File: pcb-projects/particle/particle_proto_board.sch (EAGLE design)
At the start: 53 parts, among them IC1 ATTINY20-MMH, IC2 DMC2400V, IC3 DMC2400V, SW1 SW1, SW2 SW2, SW3 SW3

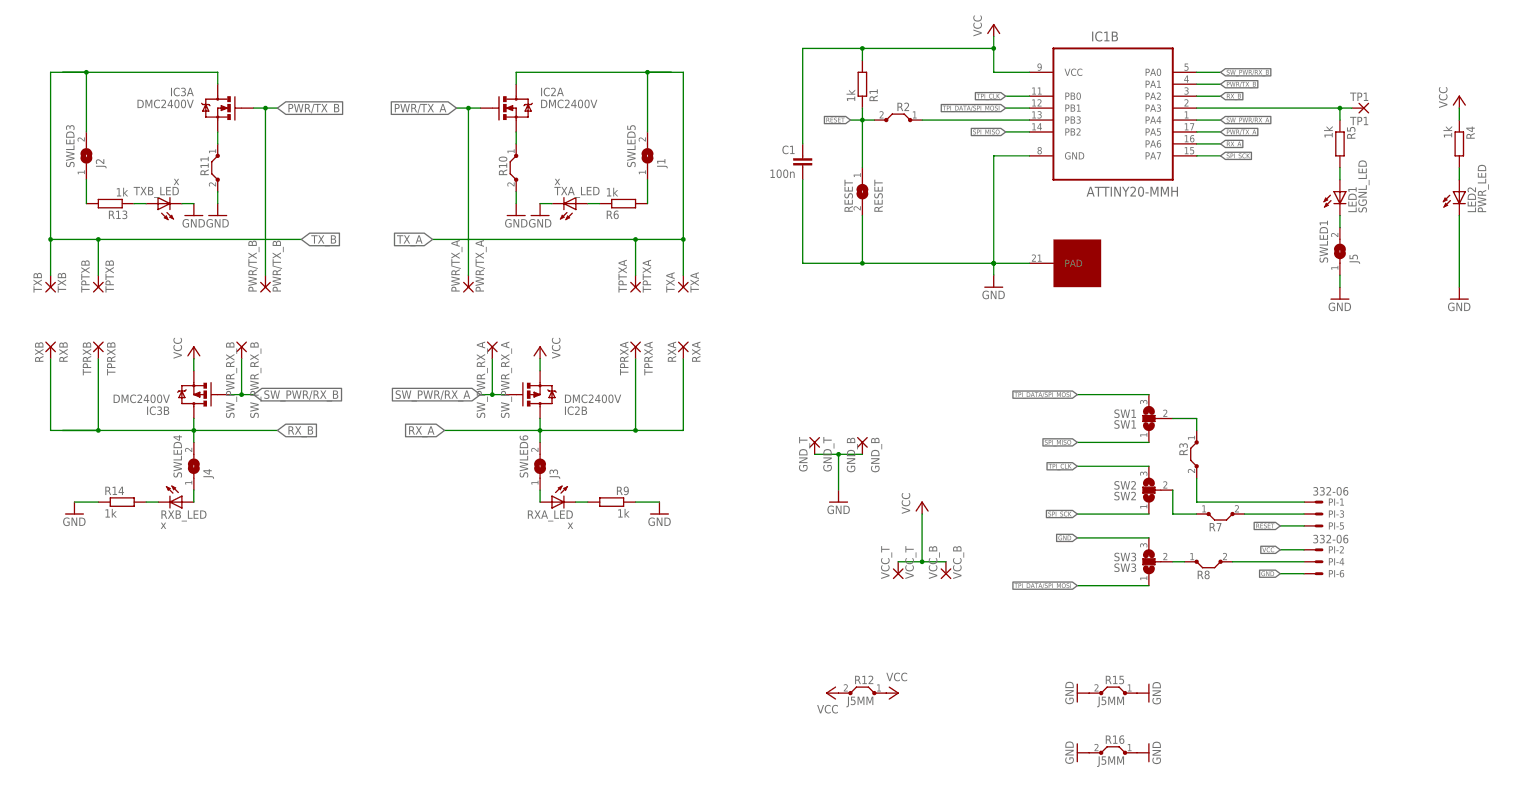
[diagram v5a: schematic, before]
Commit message: set values to all leds, renamed gnd/vcc pads, TX/RX description beside pads, placed vcc/gnd shunts exposed on schema
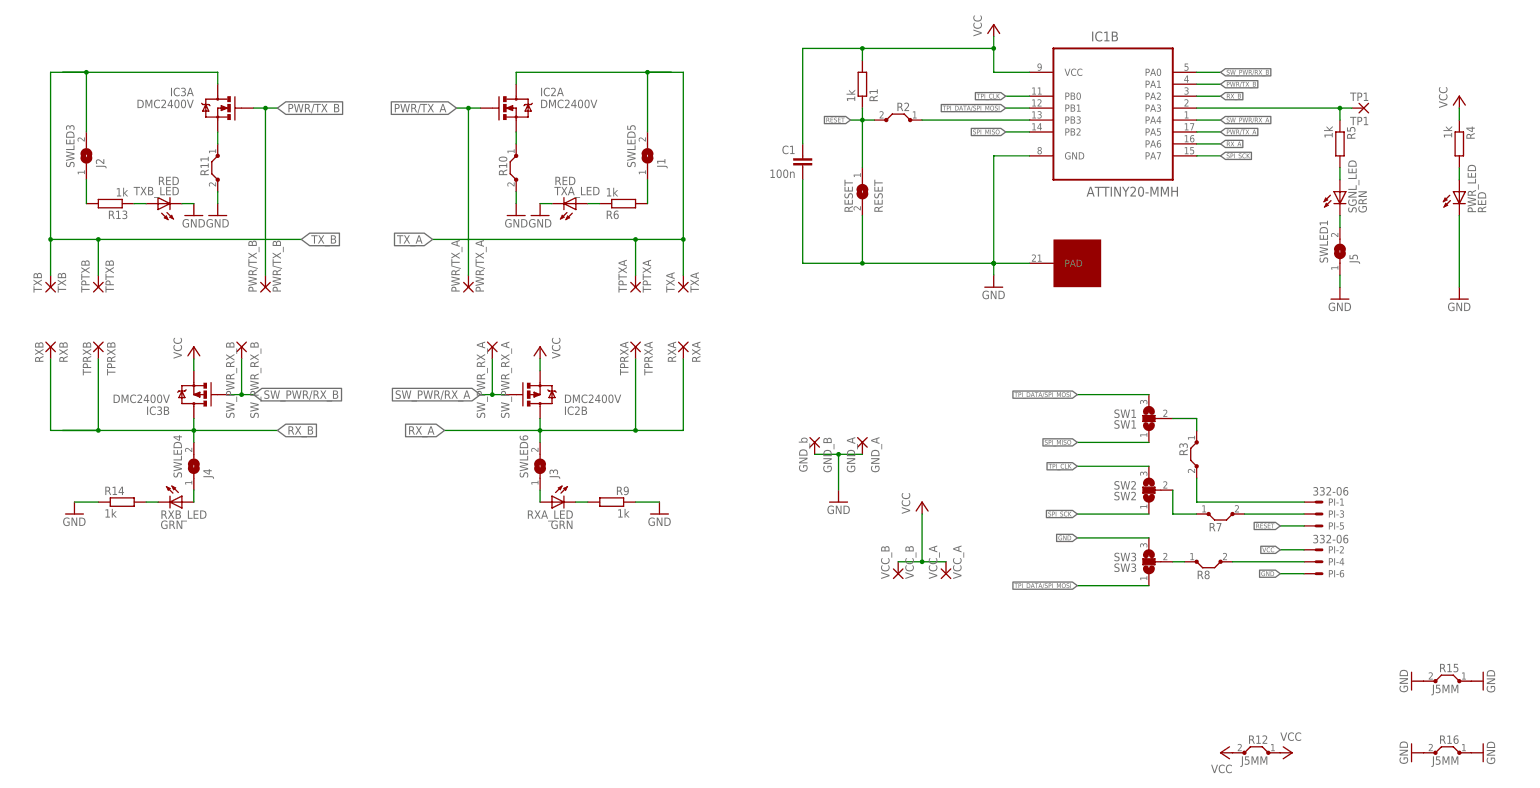
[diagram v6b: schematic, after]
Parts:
- removed GND_T: GND_T, wirepad:1,6/0,9
- removed VCC_T: VCC_T, wirepad:1,6/0,9
- added GND_A: GND_A, wirepad:1,6/0,9
- added VCC_A: VCC_A, wirepad:1,6/0,9
- GND_B: value GND_B -> GND_b
- PWR_LED: value PWR_LED -> RED
- RXA_LED, RXB_LED: value x -> GRN
- SGNL_LED: value SGNL_LED -> GRN
- TXA_LED, TXB_LED: value x -> RED
- renumbered LED1 to SGNL_LED, LED2 to PWR_LED
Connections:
- net GND: now also GND_A.P; no longer GND_T.P
- net VCC: now also VCC_A.P; no longer VCC_T.P
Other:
- note added: "SHUNTS"
- moved on the sheet: GND_B, R12, R15, R16, VCC_B
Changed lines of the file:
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@@
 <part name="R5" library="rcl" deviceset="R-EU_" device="R2010" value="1k"/>
 <part name="GND16" library="supply1" deviceset="GND" device=""/>
-<part name="LED1" library="led" deviceset="LED" device="SML1206" value="SGNL_LED"/>
+<part name="SGNL_LED" library="led" deviceset="LED" device="SML1206" value="GRN"/>
 <part name="P+2" library="supply1" deviceset="VCC" device=""/>
 <part name="IC3" library="diodes" deviceset="DMC2400V" device=""/>
@@
 <part name="R13" library="rcl" deviceset="R-EU_" device="R2010" value="1k"/>
 <part name="GND4" library="supply1" deviceset="GND" device=""/>
-<part name="TXB_LED" library="led" deviceset="LED" device="SML1206" value="x"/>
-<part name="RXB_LED" library="led" deviceset="LED" device="SML1206" value="x"/>
+<part name="TXB_LED" library="led" deviceset="LED" device="SML1206" value="RED"/>
+<part name="RXB_LED" library="led" deviceset="LED" device="SML1206" value="GRN"/>
 <part name="R14" library="rcl" deviceset="R-EU_" device="R2010" value="1k"/>
 <part name="GND5" library="supply1" deviceset="GND" device=""/>
@@
 <part name="R6" library="rcl" deviceset="R-EU_" device="R2010" value="1k"/>
 <part name="GND6" library="supply1" deviceset="GND" device=""/>
-<part name="TXA_LED" library="led" deviceset="LED" device="SML1206" value="x"/>
-<part name="RXA_LED" library="led" deviceset="LED" device="SML1206" value="x"/>
+<part name="TXA_LED" library="led" deviceset="LED" device="SML1206" value="RED"/>
+<part name="RXA_LED" library="led" deviceset="LED" device="SML1206" value="GRN"/>
 <part name="R9" library="rcl" deviceset="R-EU_" device="R2010" value="1k"/>
 <part name="GND7" library="supply1" deviceset="GND" device=""/>
@@
 <part name="GND2" library="supply1" deviceset="GND" device=""/>
 <part name="RESET" library="jumper" deviceset="SJ" device="" value="RESET"/>
+<part name="VCC_A" library="wirepad" deviceset="1,6/0,9" device="" value="VCC_A"/>
 <part name="VCC_B" library="wirepad" deviceset="1,6/0,9" device="" value="VCC_B"/>
-<part name="VCC_T" library="wirepad" deviceset="1,6/0,9" device="" value="VCC_T"/>
-<part name="GND_B" library="wirepad" deviceset="1,6/0,9" device="" value="GND_B"/>
-<part name="GND_T" library="wirepad" deviceset="1,6/0,9" device="" value="GND_T"/>
+<part name="GND_A" library="wirepad" deviceset="1,6/0,9" device="" value="GND_A"/>
+<part name="GND_B" library="wirepad" deviceset="1,6/0,9" device="" value="GND_b"/>
 <part name="RXB" library="wirepad" deviceset="1,6/0,9" device="" value="RXB"/>
 <part name="TXB" library="wirepad" deviceset="1,6/0,9" device="" value="TXB"/>
@@
 <part name="R4" library="rcl" deviceset="R-EU_" device="R2010" value="1k"/>
 <part name="GND8" library="supply1" deviceset="GND" device=""/>
-<part name="LED2" library="led" deviceset="LED" device="SML1206" value="PWR_LED"/>
+<part name="PWR_LED" library="led" deviceset="LED" device="SML1206" value="RED"/>
 <part name="P+3" library="supply1" deviceset="VCC" device=""/>
 <part name="R11" library="jumper" deviceset="J" device="5MM" value=""/>
@@
 SW2 | 2-3 | 1-2
 SW3 | 2-3 | 1-2</text>
+<wire x1="43.18" y1="-93.98" x2="210.82" y2="-93.98" width="0.3048" layer="108"/>
+<wire x1="43.18" y1="-129.54" x2="210.82" y2="-129.54" width="0.3048" layer="108"/>
+<wire x1="43.18" y1="-129.54" x2="43.18" y2="-93.98" width="0.3048" layer="108"/>
+<wire x1="210.82" y1="-129.54" x2="210.82" y2="-93.98" width="0.3048" layer="108"/>
+<text x="50.8" y="-101.6" size="2.54" layer="108" font="vector">SHUNTS</text>
 </plain>
 <instances>
@@
 <instance part="R5" gate="G$1" x="167.64" y="10.16" rot="R270"/>
 <instance part="GND16" gate="1" x="167.64" y="-22.86"/>
-<instance part="LED1" gate="G$1" x="167.64" y="0"/>
+<instance part="SGNL_LED" gate="G$1" x="167.64" y="0"/>
 <instance part="P+2" gate="VCC" x="93.98" y="35.56"/>
 <instance part="IC3" gate="A" x="-71.12" y="17.78" rot="MR0"/>
@@
 <instance part="GND2" gate="1" x="60.96" y="-66.04" rot="MR0"/>
 <instance part="RESET" gate="1" x="66.04" y="0" rot="R270"/>
-<instance part="VCC_B" gate="1" x="83.82" y="-81.28" rot="R90"/>
-<instance part="VCC_T" gate="1" x="73.66" y="-81.28" rot="R90"/>
-<instance part="GND_B" gate="1" x="66.04" y="-53.34" rot="R270"/>
-<instance part="GND_T" gate="1" x="55.88" y="-53.34" rot="R270"/>
+<instance part="VCC_A" gate="1" x="83.82" y="-81.28" rot="R90"/>
+<instance part="VCC_B" gate="1" x="73.66" y="-81.28" rot="R90"/>
+<instance part="GND_A" gate="1" x="66.04" y="-53.34" rot="R270"/>
+<instance part="GND_B" gate="1" x="55.88" y="-53.34" rot="R270"/>
 <instance part="RXB" gate="1" x="-106.68" y="-33.02" rot="R270"/>
 <instance part="TXB" gate="1" x="-106.68" y="-20.32" rot="R90"/>
@@
 <instance part="R4" gate="G$1" x="193.04" y="10.16" rot="R270"/>
 <instance part="GND8" gate="1" x="193.04" y="-22.86"/>
-<instance part="LED2" gate="G$1" x="193.04" y="0"/>
+<instance part="PWR_LED" gate="G$1" x="193.04" y="0"/>
 <instance part="P+3" gate="VCC" x="193.04" y="20.32"/>
 <instance part="R11" gate="1" x="-71.12" y="5.08" rot="MR270"/>
-<instance part="P+5" gate="VCC" x="58.42" y="-106.68" rot="R90"/>
-<instance part="P+7" gate="VCC" x="73.66" y="-106.68" rot="R270"/>
-<instance part="R12" gate="1" x="66.04" y="-106.68" rot="MR0"/>
-<instance part="GND9" gate="1" x="111.76" y="-106.68" rot="R270"/>
-<instance part="GND10" gate="1" x="127" y="-106.68" rot="R90"/>
-<instance part="GND11" gate="1" x="111.76" y="-119.38" rot="R270"/>
-<instance part="GND12" gate="1" x="127" y="-119.38" rot="R90"/>
-<instance part="R16" gate="1" x="119.38" y="-119.38" rot="MR0"/>
-<instance part="R15" gate="1" x="119.38" y="-106.68" rot="MR0"/>
+<instance part="P+5" gate="VCC" x="142.24" y="-119.38" rot="R90"/>
+<instance part="P+7" gate="VCC" x="157.48" y="-119.38" rot="R270"/>
+<instance part="R12" gate="1" x="149.86" y="-119.38" rot="MR0"/>
+<instance part="GND9" gate="1" x="182.88" y="-104.14" rot="R270"/>
+<instance part="GND10" gate="1" x="198.12" y="-104.14" rot="R90"/>
+<instance part="GND11" gate="1" x="182.88" y="-119.38" rot="R270"/>
+<instance part="GND12" gate="1" x="198.12" y="-119.38" rot="R90"/>
+<instance part="R16" gate="1" x="190.5" y="-119.38" rot="MR0"/>
+<instance part="R15" gate="1" x="190.5" y="-104.14" rot="MR0"/>
 </instances>
 <busses>
@@
 <pinref part="GND2" gate="1" pin="GND"/>
 <wire x1="60.96" y1="-63.5" x2="60.96" y2="-55.88" width="0.1524" layer="91"/>
-<pinref part="GND_T" gate="1" pin="P"/>
 <pinref part="GND_B" gate="1" pin="P"/>
+<pinref part="GND_A" gate="1" pin="P"/>
 <wire x1="55.88" y1="-55.88" x2="60.96" y2="-55.88" width="0.1524" layer="91"/>
 <junction x="60.96" y="-55.88"/>
@@
 <segment>
 <pinref part="GND8" gate="1" pin="GND"/>
-<pinref part="LED2" gate="G$1" pin="C"/>
+<pinref part="PWR_LED" gate="G$1" pin="C"/>
 <wire x1="193.04" y1="-5.08" x2="193.04" y2="-20.32" width="0.1524" layer="91"/>
 </segment>
@@
 </segment>
 <segment>
-<pinref part="VCC_T" gate="1" pin="P"/>
 <pinref part="VCC_B" gate="1" pin="P"/>
+<pinref part="VCC_A" gate="1" pin="P"/>
 <wire x1="73.66" y1="-78.74" x2="78.74" y2="-78.74" width="0.1524" layer="91"/>
 <pinref part="P+4" gate="VCC" pin="VCC"/>
@@
 <segment>
 <pinref part="R5" gate="G$1" pin="2"/>
-<pinref part="LED1" gate="G$1" pin="A"/>
+<pinref part="SGNL_LED" gate="G$1" pin="A"/>
 <wire x1="167.64" y1="5.08" x2="167.64" y2="2.54" width="0.1524" layer="91"/>
 </segment>
@@
 <net name="N$23" class="0">
 <segment>
-<pinref part="LED1" gate="G$1" pin="C"/>
+<pinref part="SGNL_LED" gate="G$1" pin="C"/>
 <pinref part="SWLED1" gate="1" pin="2"/>
 <wire x1="167.64" y1="-5.08" x2="167.64" y2="-7.62" width="0.1524" layer="91"/>
@@
 <segment>
 <pinref part="R4" gate="G$1" pin="2"/>
-<pinref part="LED2" gate="G$1" pin="A"/>
+<pinref part="PWR_LED" gate="G$1" pin="A"/>
 <wire x1="193.04" y1="5.08" x2="193.04" y2="2.54" width="0.1524" layer="91"/>
 </segment>

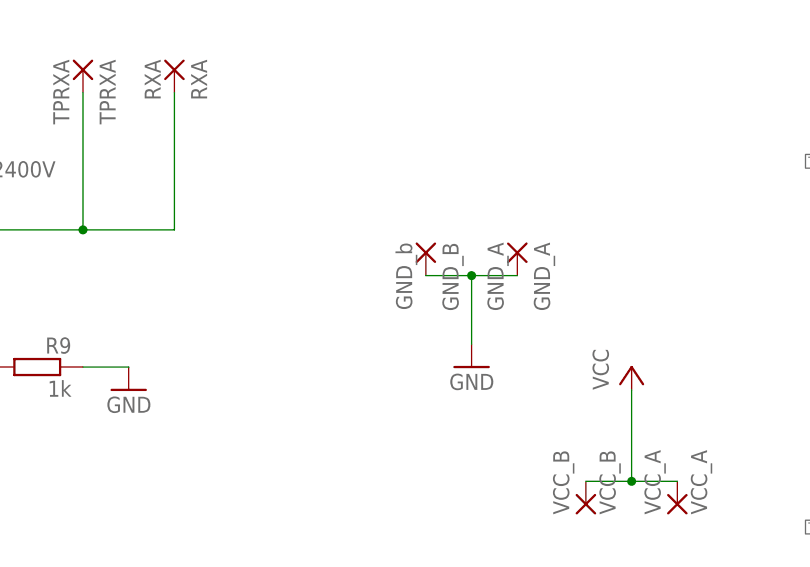
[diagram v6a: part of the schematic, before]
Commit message: fixed typo in schema
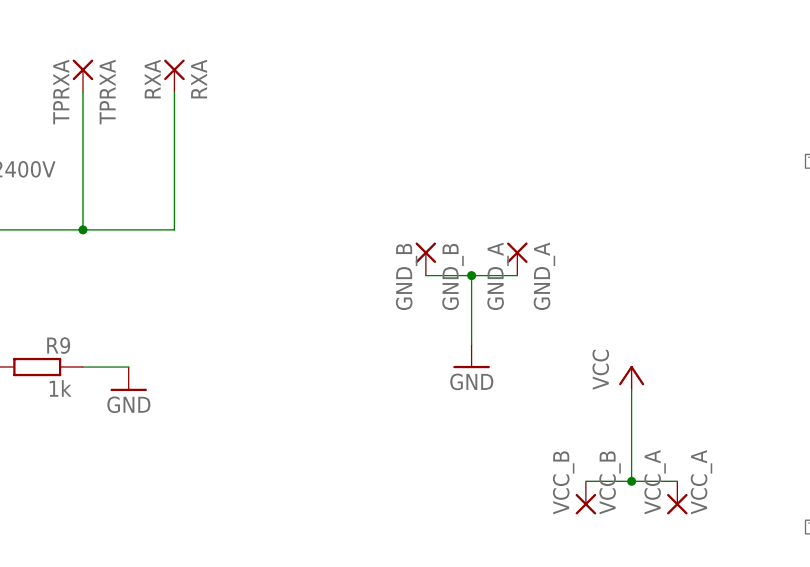
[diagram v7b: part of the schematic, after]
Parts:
- GND_B: value GND_b -> GND_B
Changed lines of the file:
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@@
 <part name="VCC_B" library="wirepad" deviceset="1,6/0,9" device="" value="VCC_B"/>
 <part name="GND_A" library="wirepad" deviceset="1,6/0,9" device="" value="GND_A"/>
-<part name="GND_B" library="wirepad" deviceset="1,6/0,9" device="" value="GND_b"/>
+<part name="GND_B" library="wirepad" deviceset="1,6/0,9" device="" value="GND_B"/>
 <part name="RXB" library="wirepad" deviceset="1,6/0,9" device="" value="RXB"/>
 <part name="TXB" library="wirepad" deviceset="1,6/0,9" device="" value="TXB"/>

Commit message: solved #34, solved #33, solved #32
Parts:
- RESET, SWLED1, SWLED3, SWLED4, SWLED5, SWLED6: device jumper:SJ -> jumper-switches:SJ
- SW1, SW2, SW3: device jumper:SJ2W -> jumper-switches:SJ2W
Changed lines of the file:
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@@
 <part name="SW_PWR_RX_B" library="wirepad" deviceset="1,6/0,9" device="" value="SW_PWR_RX_B"/>
 <part name="TPRXB" library="wirepad" deviceset="1,6/0,9" device="" value="TPRXB"/>
-<part name="SWLED5" library="jumper" deviceset="SJ" device="" value="J1"/>
-<part name="SWLED3" library="jumper" deviceset="SJ" device="" value="J2"/>
-<part name="SWLED4" library="jumper" deviceset="SJ" device="" value="J4"/>
-<part name="SWLED6" library="jumper" deviceset="SJ" device="" value="J3"/>
-<part name="SWLED1" library="jumper" deviceset="SJ" device="" value="J5"/>
-<part name="SW2" library="jumper" deviceset="SJ2W" device="" value="SW2"/>
-<part name="SW3" library="jumper" deviceset="SJ2W" device="" value="SW3"/>
-<part name="SW1" library="jumper" deviceset="SJ2W" device="" value="SW1"/>
+<part name="SWLED5" library="jumper-switches" deviceset="SJ" device="" value="J1"/>
+<part name="SWLED3" library="jumper-switches" deviceset="SJ" device="" value="J2"/>
+<part name="SWLED4" library="jumper-switches" deviceset="SJ" device="" value="J4"/>
+<part name="SWLED6" library="jumper-switches" deviceset="SJ" device="" value="J3"/>
+<part name="SWLED1" library="jumper-switches" deviceset="SJ" device="" value="J5"/>
+<part name="SW2" library="jumper-switches" deviceset="SJ2W" device="" value="SW2"/>
+<part name="SW3" library="jumper-switches" deviceset="SJ2W" device="" value="SW3"/>
+<part name="SW1" library="jumper-switches" deviceset="SJ2W" device="" value="SW1"/>
 <part name="P+4" library="supply1" deviceset="VCC" device=""/>
 <part name="GND2" library="supply1" deviceset="GND" device=""/>
-<part name="RESET" library="jumper" deviceset="SJ" device="" value="RESET"/>
+<part name="RESET" library="jumper-switches" deviceset="SJ" device="" value="RESET"/>
 <part name="VCC_A" library="wirepad" deviceset="1,6/0,9" device="" value="VCC_A"/>
 <part name="VCC_B" library="wirepad" deviceset="1,6/0,9" device="" value="VCC_B"/>
